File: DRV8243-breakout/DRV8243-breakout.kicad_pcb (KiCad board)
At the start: 2 copper layers, 50 x 40 mm, 27 parts, among them J1 Vin, J2 Motor_Output, J3 Conn_01x11_Pin, J4 Motor_Output, Q1 PMOS-AOD409, U1 PDRV8243HRXYQ1, U2 PDRV8243HRXYQ1

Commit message: beginning routing
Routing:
- net OUT2: track 0.00 -> 32.2 mm
- net OUT4: track 0.00 -> 30.9 mm
- net OUT3: track 0.00 -> 23.1 mm
- net OUT1: track 0.00 -> 22.5 mm
- net VM: track 44.8 -> 35.5 mm, vias 6 -> 0
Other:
- board text added: "ala"
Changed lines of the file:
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@@
 		(layer "Edge.Cuts")
+	)
+	(gr_text "ala"
+		(at 154.2 109 0)
+		(layer "B.Cu")
+		(effects
+			(font
+				(size 1.5 1.5)
+				(thickness 0.3)
+				(bold yes)
+			)
+			(justify left bottom mirror)
+		)
 	)
 	(segment
@@
 		(net 2)
 	)
-	(via
-		(at 174.150001 93.2)
-		(size 0.6)
-		(drill 0.3)
-		(layers "F.Cu" "B.Cu")
-		(net 2)
-	)
-	(via
-		(at 174.2 93.8)
-		(size 0.6)
-		(drill 0.3)
-		(layers "F.Cu" "B.Cu")
-		(net 2)
-	)
-	(via
-		(at 174.150001 94.4)
-		(size 0.6)
-		(drill 0.3)
-		(layers "F.Cu" "B.Cu")
-		(net 2)
-	)
-	(via
-		(at 186.650001 94)
-		(size 0.6)
-		(drill 0.3)
-		(layers "F.Cu" "B.Cu")
-		(net 2)
-	)
-	(via
-		(at 186.650001 94.5)
-		(size 0.6)
-		(drill 0.3)
-		(layers "F.Cu" "B.Cu")
-		(net 2)
-	)
-	(via
-		(at 186.650001 93.5)
-		(size 0.6)
-		(drill 0.3)
-		(layers "F.Cu" "B.Cu")
-		(net 2)
-	)
-	(segment
-		(start 174.150001 98.000001)
-		(end 174.150001 97)
-		(width 0.6)
-		(layer "B.Cu")
-		(net 2)
-	)
-	(segment
-		(start 174.150001 95.999999)
-		(end 174.150001 97)
-		(width 0.6)
-		(layer "B.Cu")
-		(net 2)
-	)
-	(segment
-		(start 174.2 93.8)
-		(end 174.2 93.249999)
-		(width 0.6)
-		(layer "B.Cu")
-		(net 2)
-	)
-	(segment
-		(start 174.150001 93.849999)
-		(end 174.2 93.8)
-		(width 0.6)
-		(layer "B.Cu")
-		(net 2)
-	)
-	(segment
-		(start 174.150001 94.4)
-		(end 174.150001 93.849999)
-		(width 0.6)
-		(layer "B.Cu")
-		(net 2)
-	)
-	(segment
-		(start 174.150001 95.999999)
-		(end 174.150001 94.4)
-		(width 0.6)
-		(layer "B.Cu")
-		(net 2)
-	)
-	(segment
-		(start 174.2 93.249999)
-		(end 174.150001 93.2)
-		(width 0.6)
-		(layer "B.Cu")
-		(net 2)
-	)
-	(segment
-		(start 186.650001 98.000001)
-		(end 186.650001 94.5)
-		(width 0.6)
-		(layer "B.Cu")
-		(net 2)
-	)
-	(segment
-		(start 186.650001 94.5)
-		(end 186.650001 93.5)
-		(width 0.6)
-		(layer "B.Cu")
-		(net 2)
-	)
 	(segment
 		(start 154 77.74)
@@
 		(net 5)
 	)
+	(segment
+		(start 169.8 94)
+		(end 169.8 97.2)
+		(width 3)
+		(layer "B.Cu")
+		(net 6)
+	)
+	(segment
+		(start 172.551 99.951)
+		(end 174.8 99.951)
+		(width 3)
+		(layer "B.Cu")
+		(net 6)
+	)
+	(segment
+		(start 169.8 97.2)
+		(end 172.551 99.951)
+		(width 3)
+		(layer "B.Cu")
+		(net 6)
+	)
+	(segment
+		(start 179 84.8)
+		(end 169.8 94)
+		(width 3)
+		(layer "B.Cu")
+		(net 6)
+	)
+	(segment
+		(start 179 75)
+		(end 179 84.8)
+		(width 3)
+		(layer "B.Cu")
+		(net 6)
+	)
+	(segment
+		(start 184 85.649)
+		(end 175.6 94.049)
+		(width 3)
+		(layer "B.Cu")
+		(net 7)
+	)
+	(segment
+		(start 184 75)
+		(end 184 85.649)
+		(width 3)
+		(layer "B.Cu")
+		(net 7)
+	)
+	(segment
+		(start 191 75)
+		(end 189 77)
+		(width 3)
+		(layer "B.Cu")
+		(net 20)
+	)
+	(segment
+		(start 185.351 99.951)
+		(end 187.2 99.951)
+		(width 3)
+		(layer "B.Cu")
+		(net 20)
+	)
+	(segment
+		(start 183.2 97.8)
+		(end 185.351 99.951)
+		(width 3)
+		(layer "B.Cu")
+		(net 20)
+	)
+	(segment
+		(start 189 88.2)
+		(end 183.2 94)
+		(width 3)
+		(layer "B.Cu")
+		(net 20)
+	)
+	(segment
+		(start 189 77)
+		(end 189 88.2)
+		(width 3)
+		(layer "B.Cu")
+		(net 20)
+	)
+	(segment
+		(start 183.2 94)
+		(end 183.2 97.8)
+		(width 3)
+		(layer "B.Cu")
+		(net 20)
+	)
+	(segment
+		(start 196 75)
+		(end 192.649 78.351)
+		(width 3)
+		(layer "B.Cu")
+		(net 21)
+	)
+	(segment
+		(start 189.308131 94.049)
+		(end 188 94.049)
+		(width 3)
+		(layer "B.Cu")
+		(net 21)
+	)
+	(segment
+		(start 192.649 90.708131)
+		(end 189.308131 94.049)
+		(width 3)
+		(layer "B.Cu")
+		(net 21)
+	)
+	(segment
+		(start 192.649 78.351)
+		(end 192.649 90.708131)
+		(width 3)
+		(layer "B.Cu")
+		(net 21)
+	)
 	(embedded_fonts no)

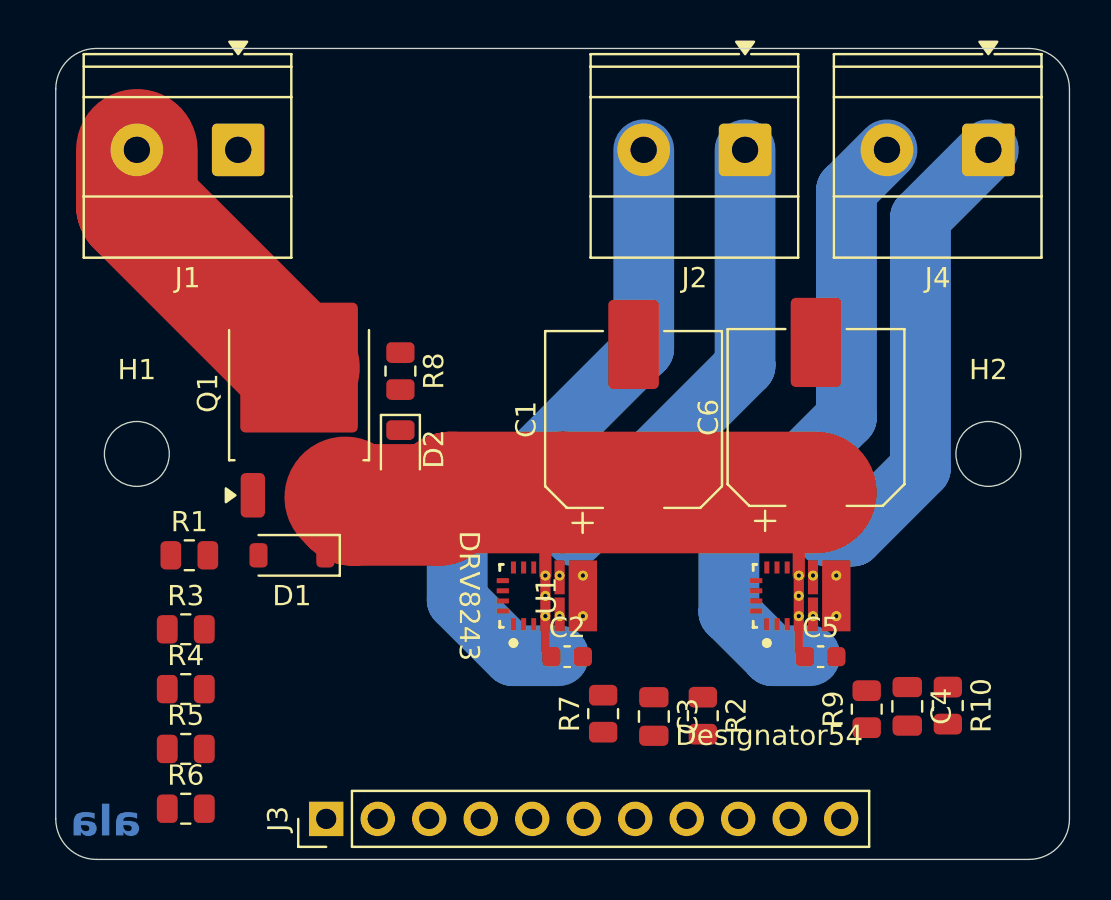
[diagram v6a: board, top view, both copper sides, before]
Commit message: Initial High Current Routing
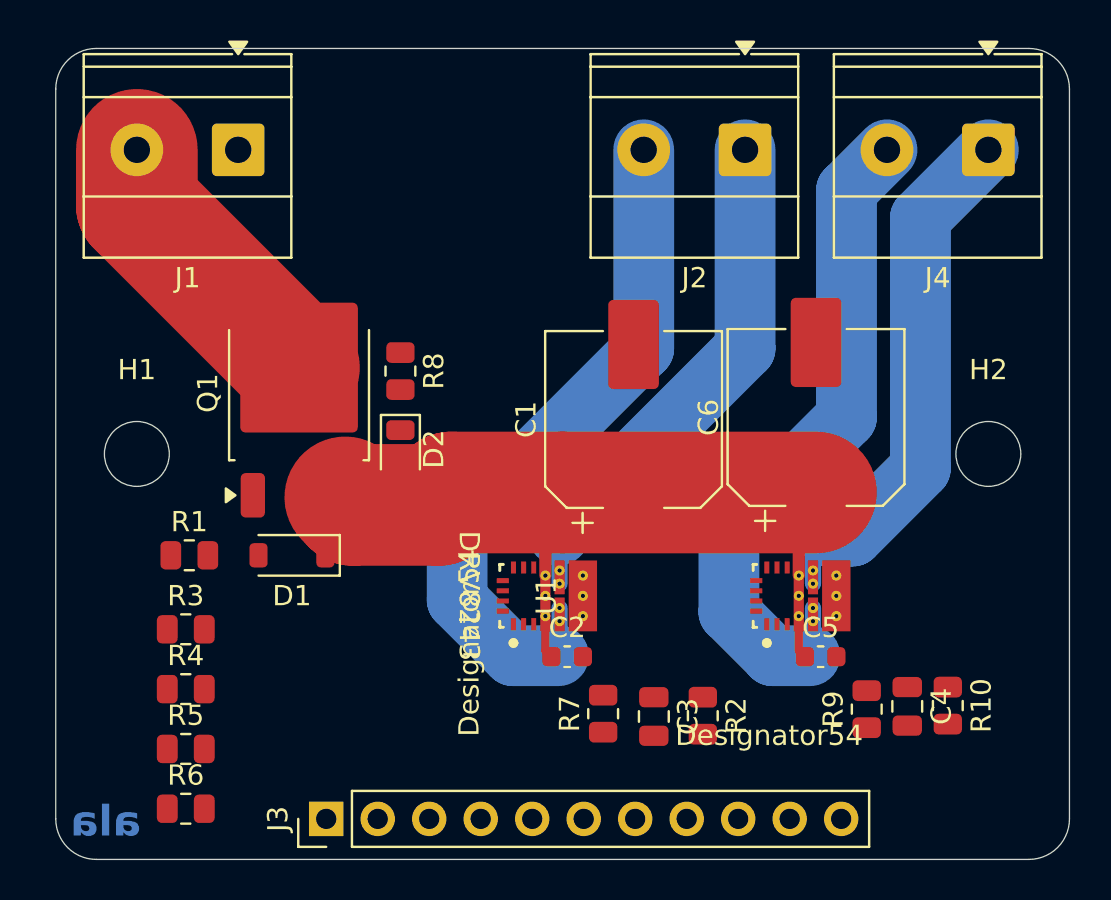
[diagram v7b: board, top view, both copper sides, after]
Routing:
- net OUT1: track 22.5 -> 25.2 mm
- net OUT3: track 23.1 -> 25.7 mm
- net OUT4: track 30.9 -> 33.5 mm
- net OUT2: track 32.2 -> 34.5 mm
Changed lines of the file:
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@@
 		)
 		(pad "18" thru_hole circle
-			(at -1.000001 0.650001 90)
+			(at -1.25 0.65 90)
 			(size 0.499999 0.499999)
 			(drill 0.2032)
@@
 			(remove_unused_layers no)
 		)
-		(pad "19" thru_hole circle
-			(at 1.000001 0.650001 90)
+		(pad "18" thru_hole circle
+			(at -0.6 0.65 90)
+			(size 0.499999 0.499999)
+			(drill 0.2032)
+			(layers "*.Cu" "*.Mask")
+			(remove_unused_layers no)
+		)
+		(pad "20" thru_hole circle
+			(at 0.6 0.65 90)
 			(size 0.499999 0.499999)
 			(drill 0.2032)
@@
 		)
 		(pad "20" thru_hole circle
-			(at 1.000001 1.799999 90)
+			(at 1.25 0.65 90)
+			(size 0.499999 0.499999)
+			(drill 0.2032)
+			(layers "*.Cu" "*.Mask")
+			(remove_unused_layers no)
+		)
+		(pad "22" thru_hole circle
+			(at -1 1.8 90)
 			(size 0.499999 0.499999)
 			(drill 0.2032)
@@
 			(remove_unused_layers no)
 		)
-		(pad "21" thru_hole circle
-			(at -1.000001 1.799999 90)
+		(pad "23" thru_hole circle
+			(at 0 1.8 90)
+			(size 0.499999 0.499999)
+			(drill 0.2032)
+			(layers "*.Cu" "*.Mask")
+			(remove_unused_layers no)
+		)
+		(pad "23" thru_hole circle
+			(at 1 1.8 90)
 			(size 0.499999 0.499999)
 			(drill 0.2032)
@@
 			)
 		)
+		(fp_text user "Designator54"
+			(at -2.311395 -3.81001 90)
+			(unlocked yes)
+			(layer "F.SilkS")
+			(effects
+				(font
+					(size 1 1)
+					(thickness 0.15)
+				)
+			)
+		)
 		(fp_text user "${REFERENCE}"
 			(at 0 0 90)
@@
 		)
 		(pad "18" thru_hole circle
-			(at -1.000001 0.650001 90)
+			(at -1.25 0.65 90)
 			(size 0.499999 0.499999)
 			(drill 0.2032)
@@
 			(remove_unused_layers no)
 		)
-		(pad "19" thru_hole circle
-			(at 1.000001 0.650001 90)
+		(pad "18" thru_hole circle
+			(at -0.6 0.65 90)
 			(size 0.499999 0.499999)
 			(drill 0.2032)
@@
 		)
 		(pad "20" thru_hole circle
-			(at 1.000001 1.799999 90)
+			(at 0.6 0.65 90)
 			(size 0.499999 0.499999)
 			(drill 0.2032)
@@
 			(remove_unused_layers no)
 		)
-		(pad "21" thru_hole circle
-			(at -1.000001 1.799999 90)
+		(pad "20" thru_hole circle
+			(at 1.25 0.65 90)
 			(size 0.499999 0.499999)
 			(drill 0.2032)
@@
 			(remove_unused_layers no)
 		)
-		(embedded_fonts no)
-		(model "${KIPRJMOD}/libraries/RXY0014A.stp"
-			(offset
-				(xyz 0 0 0)
-			)
-			(scale
-				(xyz 1 1 1)
-			)
-			(rotate
-				(xyz 0 0 0)
-			)
+		(pad "22" thru_hole circle
+			(at -1 1.8 90)
+			(size 0.499999 0.499999)
+			(drill 0.2032)
+			(layers "*.Cu" "*.Mask")
+			(remove_unused_layers no)
+		)
+		(pad "23" thru_hole circle
+			(at 0 1.8 90)
+			(size 0.499999 0.499999)
+			(drill 0.2032)
+			(layers "*.Cu" "*.Mask")
+			(remove_unused_layers no)
+		)
+		(pad "23" thru_hole circle
+			(at 1 1.8 90)
+			(size 0.499999 0.499999)
+			(drill 0.2032)
+			(layers "*.Cu" "*.Mask")
+			(remove_unused_layers no)
 		)
+		(embedded_fonts no)
 	)
 	(footprint "DRV8243:TO-252-2(DPAK)"
@@
 	)
 	(segment
+		(start 174.850001 99.900999)
+		(end 174.8 99.951)
+		(width 0.8)
+		(layer "B.Cu")
+		(net 6)
+	)
+	(segment
+		(start 174.850001 97.6)
+		(end 174.850001 99.900999)
+		(width 0.8)
+		(layer "B.Cu")
+		(net 6)
+	)
+	(segment
 		(start 179 84.8)
 		(end 169.8 94)
@@
 	)
 	(segment
-		(start 184 85.649)
-		(end 175.6 94.049)
+		(start 174.850001 96.4)
+		(end 174.850001 94.050001)
+		(width 0.8)
+		(layer "B.Cu")
+		(net 7)
+	)
+	(segment
+		(start 174.850001 94.050001)
+		(end 174.8 94)
+		(width 0.8)
+		(layer "B.Cu")
+		(net 7)
+	)
+	(segment
+		(start 184 84.8)
+		(end 174.8 94)
 		(width 3)
 		(layer "B.Cu")
@@
 	(segment
 		(start 184 75)
-		(end 184 85.649)
+		(end 184 84.8)
 		(width 3)
 		(layer "B.Cu")
@@
 	)
 	(segment
+		(start 187.350002 99.850003)
+		(end 187.450999 99.951)
+		(width 0.8)
+		(layer "B.Cu")
+		(net 20)
+	)
+	(segment
+		(start 187.350001 99.800999)
+		(end 187.2 99.951)
+		(width 0.8)
+		(layer "B.Cu")
+		(net 20)
+	)
+	(segment
 		(start 185.351 99.951)
 		(end 187.2 99.951)
@@
 	)
 	(segment
+		(start 187.350001 97.6)
+		(end 187.350001 99.800999)
+		(width 0.8)
+		(layer "B.Cu")
+		(net 20)
+	)
+	(segment
 		(start 189 77)
 		(end 189 88.2)
@@
 	)
 	(segment
+		(start 187.350001 96.4)
+		(end 187.350001 94.698999)
+		(width 0.8)
+		(layer "B.Cu")
+		(net 21)
+	)
+	(segment
 		(start 189.308131 94.049)
 		(end 188 94.049)
@@
 		(layer "B.Cu")
 		(net 21)
+	)
+	(segment
+		(start 187.350001 94.698999)
+		(end 188 94.049)
+		(width 0.8)
+		(layer "B.Cu")
+		(net 21)

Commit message: Some more routing
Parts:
- moved H2 17.9 mm to (196.8, 107.9)
- moved R3 7.77 mm to (155.9, 106.4)
- moved R6 5.22 mm to (155.9, 102.3)
- moved R4 1.39 mm to (155.9, 100.3)
- moved R5 0.56 mm to (155.9, 104.3)
- moved R7 0.50 mm to (177.0, 103.3)
- moved R2 0.41 mm to (181.8, 103.3)
- moved C3 0.41 mm to (179.4, 103.3)
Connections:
- J2 pad 1: OUT1 -> OUT2
- J2 pad 2: OUT2 -> OUT1
- J4 pad 1: OUT3 -> OUT4
- J4 pad 2: OUT4 -> OUT3
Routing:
- net IN3: track 0.00 -> 20.4 mm, vias 0 -> 2
- net MODE: track 0.00 -> 18.8 mm
- net nSLEEP: track 0.00 -> 18.3 mm, vias 0 -> 2
- net ITRIP: track 0.00 -> 18.1 mm
- net IPROPI1: track 0.00 -> 17.9 mm
- net SR: track 0.00 -> 17.5 mm
- net DIAG: track 0.00 -> 16.9 mm
- net IN2: track 0.00 -> 14.8 mm, vias 0 -> 1
- net IN4: track 0.00 -> 14.6 mm, vias 0 -> 1
- net IN1: track 0.00 -> 13.2 mm, vias 0 -> 2
- net IPROPI0: track 0.00 -> 12.1 mm
- net nFault: track 0.00 -> 6.85 mm
- net OUT3: track 25.7 -> 22.8 mm
- net OUT2: track 34.5 -> 32.2 mm
- net OUT4: track 33.5 -> 32.4 mm
